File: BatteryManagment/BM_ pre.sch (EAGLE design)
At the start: 98 parts, among them IC1 LMV321M5, U1 ATMEGA328P-AU, U2 LTC4440EMS8E-5PBF

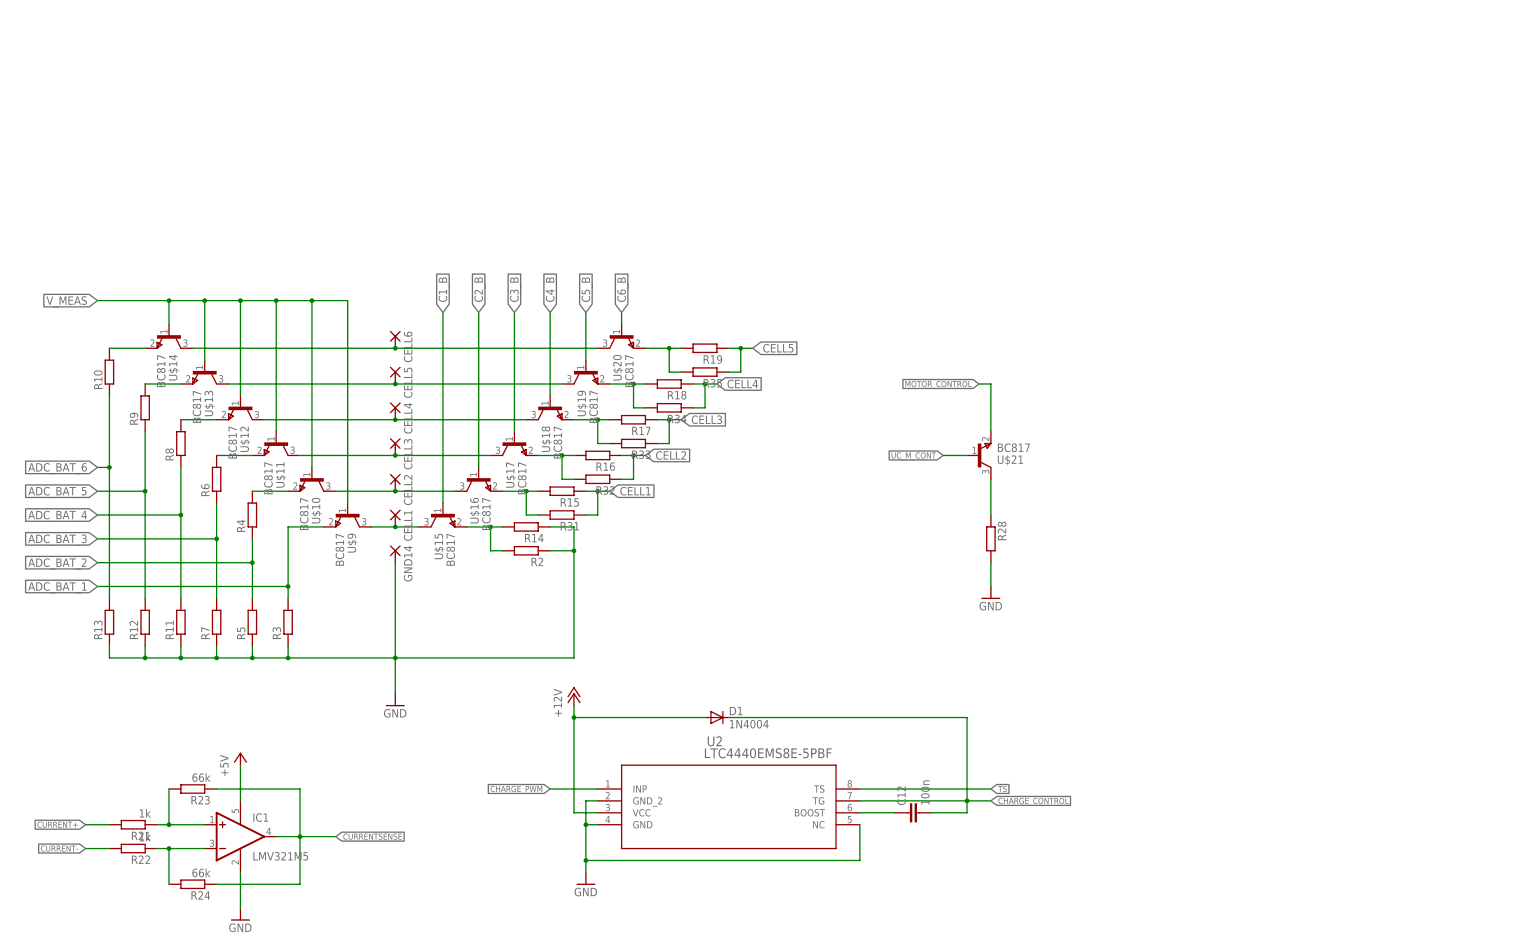
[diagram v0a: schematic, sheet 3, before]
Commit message: just for fun.... nooot
changed some parts
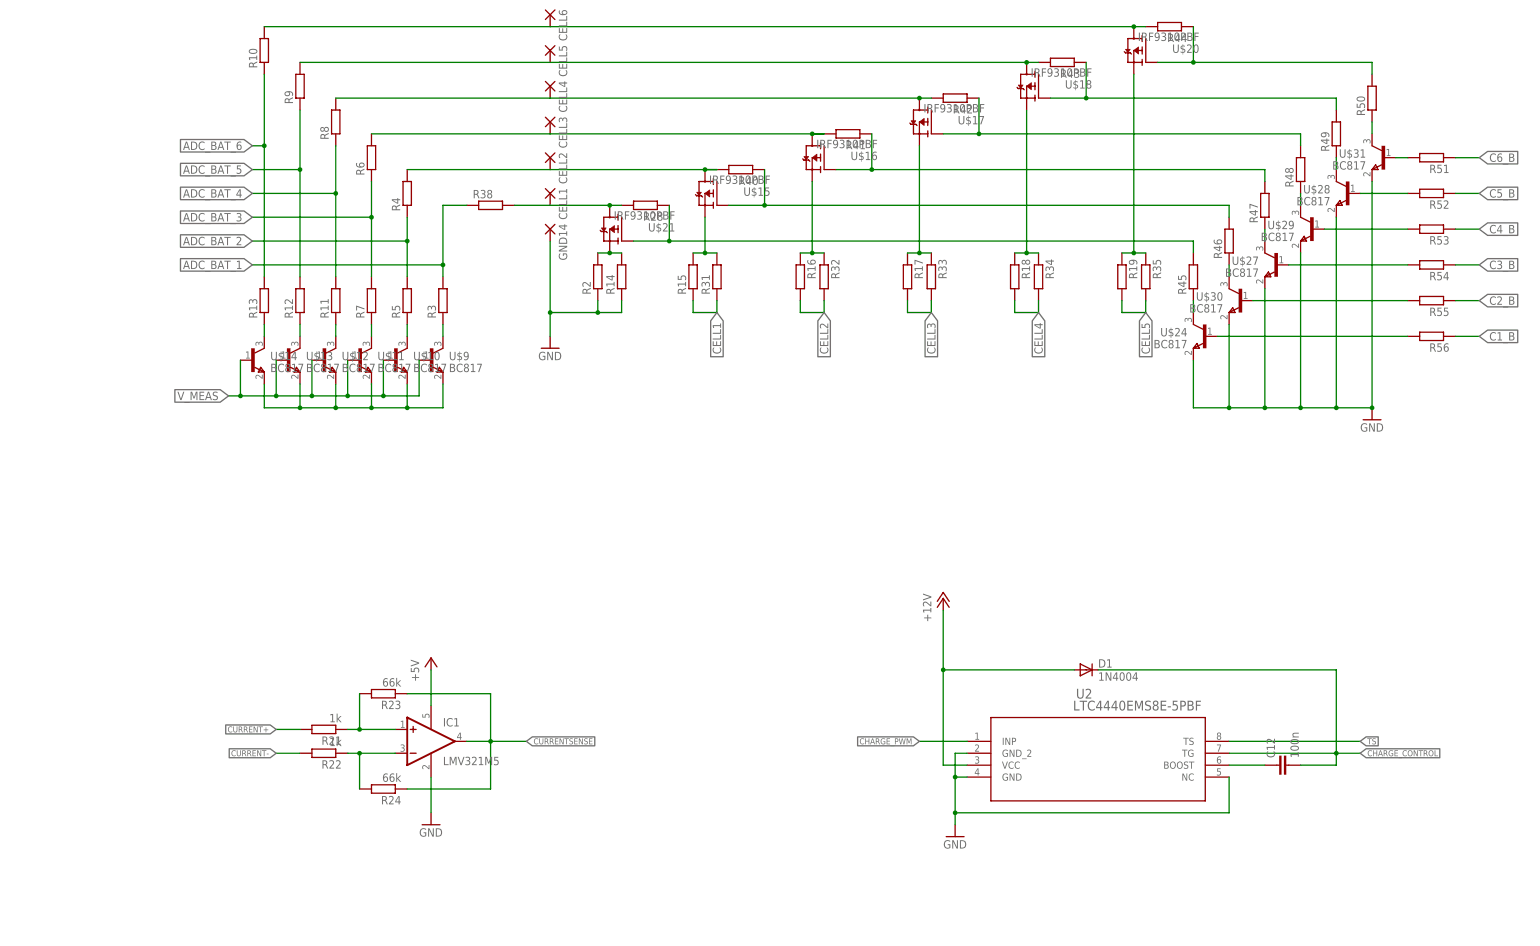
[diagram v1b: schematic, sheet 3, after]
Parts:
- added R38, R39, R40, R41, R42, R43, R44, R45, R46, R47, R48, R49, R50, R51, R52, R53, R54, R55, R56: (no value), rcl:R-EU_R0603
- added U$26, U$27, U$28, U$29, U$30, U$31: BC817, BM_pre:BC817
- U$15, U$16, U$17, U$18, U$19, U$20, U$21: value BC817 -> IRF9310PBF; device BM_pre:BC817 -> BM_pre:IRF9310PBF
- U$24: value FDN306P -> BC817; device BM_pre:FDN306P -> BM_pre:BC817
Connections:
- new net N$21: U$10.E, U$11.E, U$12.E, U$13.E, U$14.E, U$9.E
- new net N$22: R28.1, R45.2, U$21.G
- new net N$28: R40.1, R46.2, U$15.G
- new net N$29: R41.1, R47.2, U$16.G
- new net N$3: R13.1, U$14.C
- new net N$30: R42.1, R48.2, U$17.G
- new net N$31: R43.1, R49.2, U$18.G
- new net N$32: R44.1, R50.2, U$20.G
- new net N$33: R49.1, U$28.C
- new net N$34: R50.1, U$31.C
- new net N$35: R48.1, U$29.C
- new net N$36: R47.1, U$27.C
- new net N$37: R46.1, U$30.C
- new net N$38: R45.1, U$24.C
- new net N$39: R51.2, U$31.B
- new net N$40: R52.2, U$28.B
- new net N$41: R53.2, U$29.B
- new net N$42: R54.2, U$27.B
- new net N$43: R55.2, U$30.B
- new net N$44: R56.2, U$24.B
- net ADC_BAT_1: now also R38.1; no longer U$9.E
- net BATTERY+: now also U$19.S; no longer U$24.S
- net C1_B: now also R56.1; no longer U$15.B
- net C2_B: now also R55.1; no longer U$16.B
- net C3_B: now also R54.1; no longer U$17.B
- net C4_B: now also R53.1; no longer U$18.B
- net C5_B: now also R52.1; no longer U$19.B
- net C6_B: now also R51.1; no longer U$20.B
- net CELL1: now also R28.2, R38.2, U$21.D; no longer U$15.C, U$9.C
- net CELL2: now also R16.2, R32.2, R4.2, R40.2, U$15.D; no longer R16.1, R32.1, U$10.C, U$16.C
- net CELL3: now also R17.2, R33.2, R41.2, R6.2, U$16.D; no longer R17.1, R33.1, U$11.C, U$17.C
- net CELL4: now also R18.2, R34.2, R42.2, R8.2, U$17.D; no longer R18.1, R34.1, U$12.C, U$18.C
- net CELL5: now also R19.2, R35.2, R43.2, R9.2, U$18.D; no longer R19.1, R35.1, U$13.C, U$19.C
- net CELL6: now also R10.2, R44.2, U$20.D; no longer U$14.C, U$20.C
- net CHARGE_CONTROL: now also U$26.B
- net GND: now also R39.2, U$24.E, U$27.E, U$28.E, U$29.E, U$30.E, U$31.E; no longer R11.1, R12.1, R13.1, R28.2, R3.1, R5.1, R7.1
- net MOTOR_CONTROL: now also U$26.C; no longer U$21.E
- net N$10: now also R3.1, U$9.C; no longer R10.2, U$14.E
- net N$11: now also R16.1, R32.1, U$16.S; no longer R16.2, R32.2, U$17.E
- net N$12: now also R17.1, R33.1, U$17.S; no longer R17.2, R33.2, U$18.E
- net N$13: now also R18.1, R34.1, U$18.S; no longer R18.2, R34.2, U$19.E
- net N$14: now also R19.1, R35.1, U$20.S; no longer R19.2, R35.2, U$20.E
- net N$20: now also U$19.G; no longer U$24.G
- net N$26: now also R39.1, U$26.E; no longer R28.1, U$21.C
- net N$4: now also R12.1, U$13.C; no longer R4.2, U$10.E
- net N$5: now also U$21.S; no longer U$15.E
- net N$6: now also U$15.S; no longer U$16.E
- net N$7: now also R11.1, U$12.C; no longer R6.2, U$11.E
- net N$8: now also R7.1, U$11.C; no longer R8.2, U$12.E
- net N$9: now also R5.1, U$10.C; no longer R9.2, U$13.E
- net TEST: now also U$19.D; no longer U$24.D
- net UC_M_CONT: no longer U$21.B
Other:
- moved on the sheet: C12, C13, CELL1, CELL2, CELL3, CELL4, CELL5, CELL6, D1, GND14, IC1, LED1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

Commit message: V0.1 finished
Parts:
- U$15, U$16, U$17, U$18, U$20, U$21: value IRF9310PBF -> BC327; device BM_pre:IRF9310PBF -> BM_pre:BC327
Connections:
- net CELL1: now also U$15.E; no longer U$21.D
- net CELL2: now also U$16.E; no longer U$15.D
- net CELL3: now also U$17.E; no longer U$16.D
- net CELL4: now also U$18.E; no longer U$17.D
- net CELL5: now also U$20.E; no longer U$18.D
- net CELL6: now also U$21.E; no longer U$20.D
- net CHARGE_CONTROL: no longer U$26.B
- net N$11: now also U$17.C; no longer U$16.S
- net N$12: now also U$18.C; no longer U$17.S
- net N$13: now also U$20.C; no longer U$18.S
- net N$14: now also U$21.C; no longer U$20.S
- net N$22: now also U$15.B; no longer U$21.G
- net N$28: now also U$16.B; no longer U$15.G
- net N$29: now also U$17.B; no longer U$16.G
- net N$30: now also U$18.B; no longer U$17.G
- net N$31: now also U$20.B; no longer U$18.G
- net N$32: now also U$21.B; no longer U$20.G
- net N$5: now also U$15.C; no longer U$21.S
- net N$6: now also U$16.C; no longer U$15.S
- net UC_M_CONT: now also U$26.B

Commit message: Revert "Revert "Finished version v0.2""
This reverts commit 5ce350199b8ee6846b212b42396474e627ee3767.
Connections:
- net CHARGE_CONTROL: no longer D1.C
- net N$2: now also D1.C
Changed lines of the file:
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@@
-</segment>
-</net>
-<net name="CHARGE_CONTROL" class="0">
-<segment>
-<pinref part="U2" gate="A" pin="TG"/>
-<wire x1="284.48" y1="60.96" x2="307.34" y2="60.96" width="0.1524" layer="91"/>
-<label x="312.42" y="60.96" size="1.27" layer="95" xref="yes"/>
-<pinref part="C12" gate="G$1" pin="2"/>
-<wire x1="307.34" y1="60.96" x2="312.42" y2="60.96" width="0.1524" layer="91"/>
-<wire x1="299.72" y1="58.42" x2="307.34" y2="58.42" width="0.1524" layer="91"/>
-<wire x1="307.34" y1="58.42" x2="307.34" y2="60.96" width="0.1524" layer="91"/>
-<junction x="307.34" y="60.96"/>
-<pinref part="D1" gate="1" pin="C"/>
-<wire x1="256.54" y1="78.74" x2="307.34" y2="78.74" width="0.1524" layer="91"/>
-<wire x1="307.34" y1="78.74" x2="307.34" y2="60.96" width="0.1524" layer="91"/>
 </segment>
 </net>
@@
 <pinref part="C12" gate="G$1" pin="1"/>
 <pinref part="U2" gate="A" pin="BOOST"/>
-<wire x1="292.1" y1="58.42" x2="284.48" y2="58.42" width="0.1524" layer="91"/>
+<wire x1="292.1" y1="58.42" x2="287.02" y2="58.42" width="0.1524" layer="91"/>
+<pinref part="D1" gate="1" pin="C"/>
+<wire x1="287.02" y1="58.42" x2="284.48" y2="58.42" width="0.1524" layer="91"/>
+<wire x1="256.54" y1="78.74" x2="287.02" y2="78.74" width="0.1524" layer="91"/>
+<wire x1="287.02" y1="78.74" x2="287.02" y2="58.42" width="0.1524" layer="91"/>
+<junction x="287.02" y="58.42"/>
 </segment>
 </net>
@@
 </segment>
 </net>
+<net name="CHARGE_CONTROL" class="0">
+<segment>
+<wire x1="307.34" y1="60.96" x2="312.42" y2="60.96" width="0.1524" layer="91"/>
+<pinref part="C12" gate="G$1" pin="2"/>
+<wire x1="299.72" y1="58.42" x2="307.34" y2="58.42" width="0.1524" layer="91"/>
+<wire x1="307.34" y1="58.42" x2="307.34" y2="60.96" width="0.1524" layer="91"/>
+<junction x="307.34" y="60.96"/>
+<pinref part="U2" gate="A" pin="TG"/>
+<wire x1="284.48" y1="60.96" x2="307.34" y2="60.96" width="0.1524" layer="91"/>
+<label x="312.42" y="60.96" size="1.27" layer="95" xref="yes"/>
+</segment>
+</net>

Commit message: schematic up to date
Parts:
- added R57: 10k, rcl:R-EU_R0603
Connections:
- new net N$45: R57.2, U$26.B
- net UC_M_CONT: now also R57.1; no longer U$26.B
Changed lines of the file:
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@@
 <part name="U$20" library="BM_pre" deviceset="BC327" device=""/>
 <part name="U$21" library="BM_pre" deviceset="BC327" device=""/>
+<part name="R57" library="rcl" deviceset="R-EU_" device="R0603" value="10k"/>
 </parts>
 <sheets>
@@
 <instance part="GND24" gate="1" x="233.68" y="86.36"/>
 <instance part="R39" gate="G$1" x="233.68" y="99.06" rot="R270"/>
+<instance part="R57" gate="G$1" x="220.98" y="116.84"/>
 </instances>
 <busses>
@@
 </segment>
 <segment>
-<wire x1="228.6" y1="116.84" x2="223.52" y2="116.84" width="0.1524" layer="91"/>
-<label x="223.52" y="116.84" size="1.27" layer="95" rot="R180" xref="yes"/>
-<pinref part="U$26" gate="G$1" pin="B"/>
+<label x="213.36" y="116.84" size="1.27" layer="95" rot="R180" xref="yes"/>
+<pinref part="R57" gate="G$1" pin="1"/>
+<wire x1="215.9" y1="116.84" x2="213.36" y2="116.84" width="0.1524" layer="91"/>
 </segment>
 </net>
@@
 </segment>
 </net>
+<net name="N$45" class="0">
+<segment>
+<pinref part="U$26" gate="G$1" pin="B"/>
+<pinref part="R57" gate="G$1" pin="2"/>
+<wire x1="226.06" y1="116.84" x2="228.6" y2="116.84" width="0.1524" layer="91"/>
+</segment>
+</net>
